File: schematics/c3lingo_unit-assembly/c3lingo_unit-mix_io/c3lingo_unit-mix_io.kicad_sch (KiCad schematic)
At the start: 45 parts, among them J201 Stage Line-In, J202 Mix Line-Out, J203 PowerSupply, J204 Ch1, J205 Ch2, J206 Ch3, SW201 GND Lift, U201 LM833-N, U202 DRV135UA, U203 LM833-N

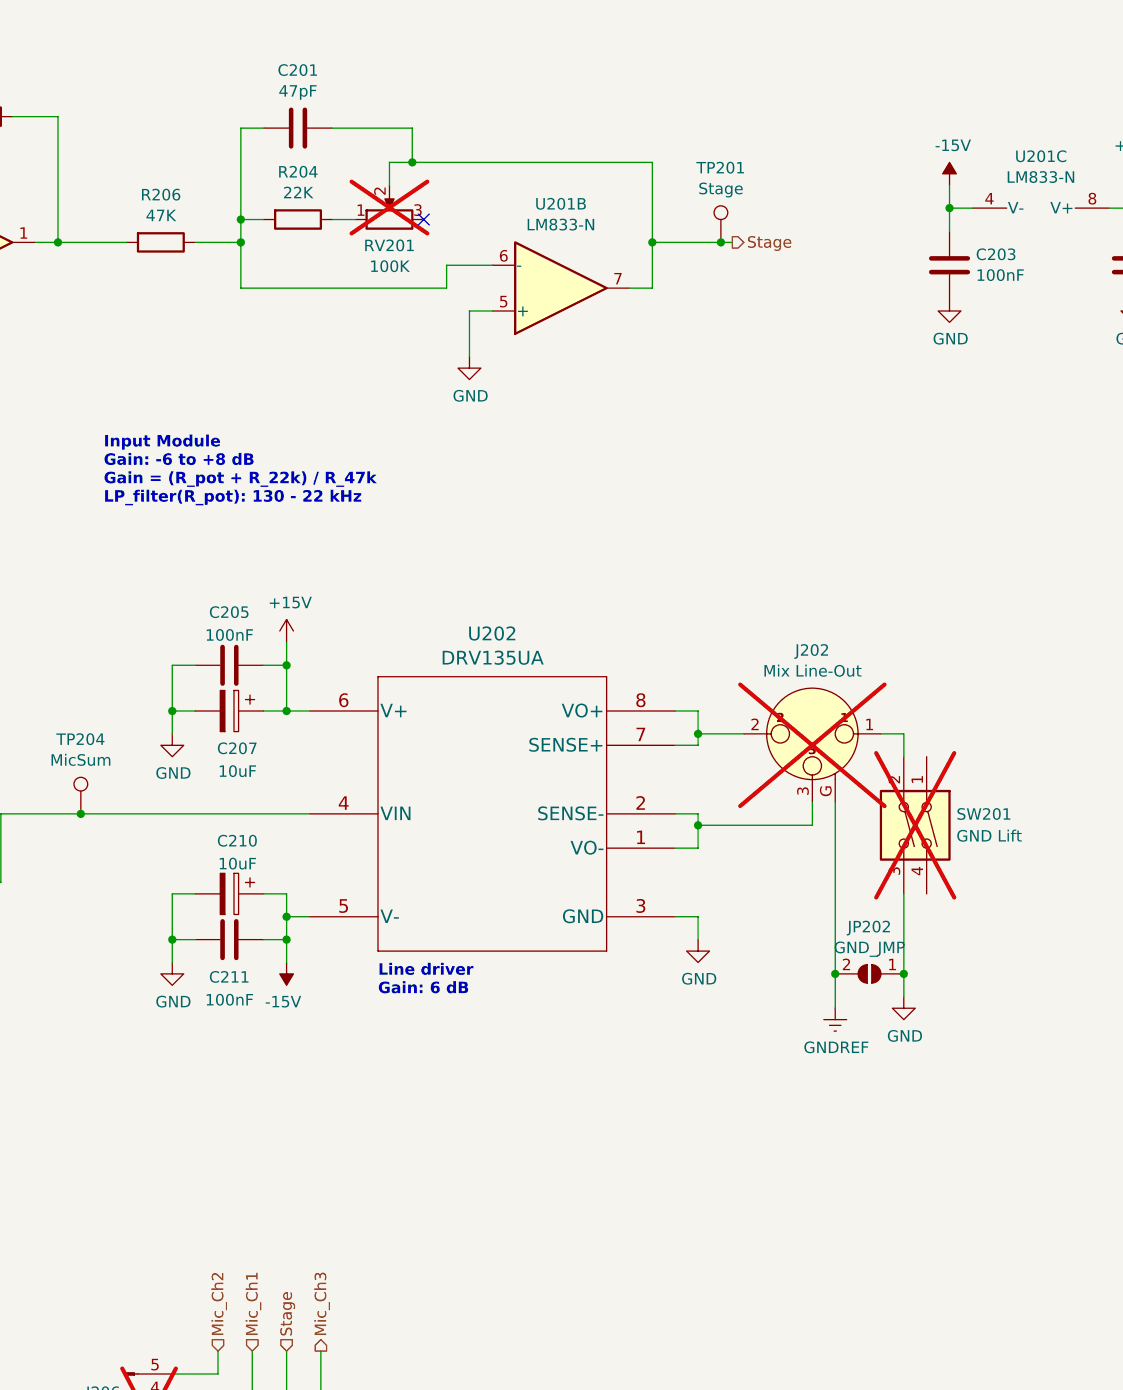
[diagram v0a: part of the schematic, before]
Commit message: Add rework to fix VU meter, muting delay, LP filters
Note: PCB files were not upated!

Changes/ required manual rework:
- Replace C314 with 100nF to reduce muting fade time
- Replace C301 with 680pF to have a 12 kHz low-pass filter on headphones
- Replace R309, R232, R335 to fix VU meter range (steps are a bit wonky
  afterwards, but top (and bottom) range are a lot more save now)
- Add 220pF in parallel to R602 to have a 10 kHz low-pass on microphone input

More rework is optional:
- Replace RV201 with a 10k (fixed) resistor (adjustment is not necessary)
- Replace R303 with 1k to reduce gain range from 45 to 34dB
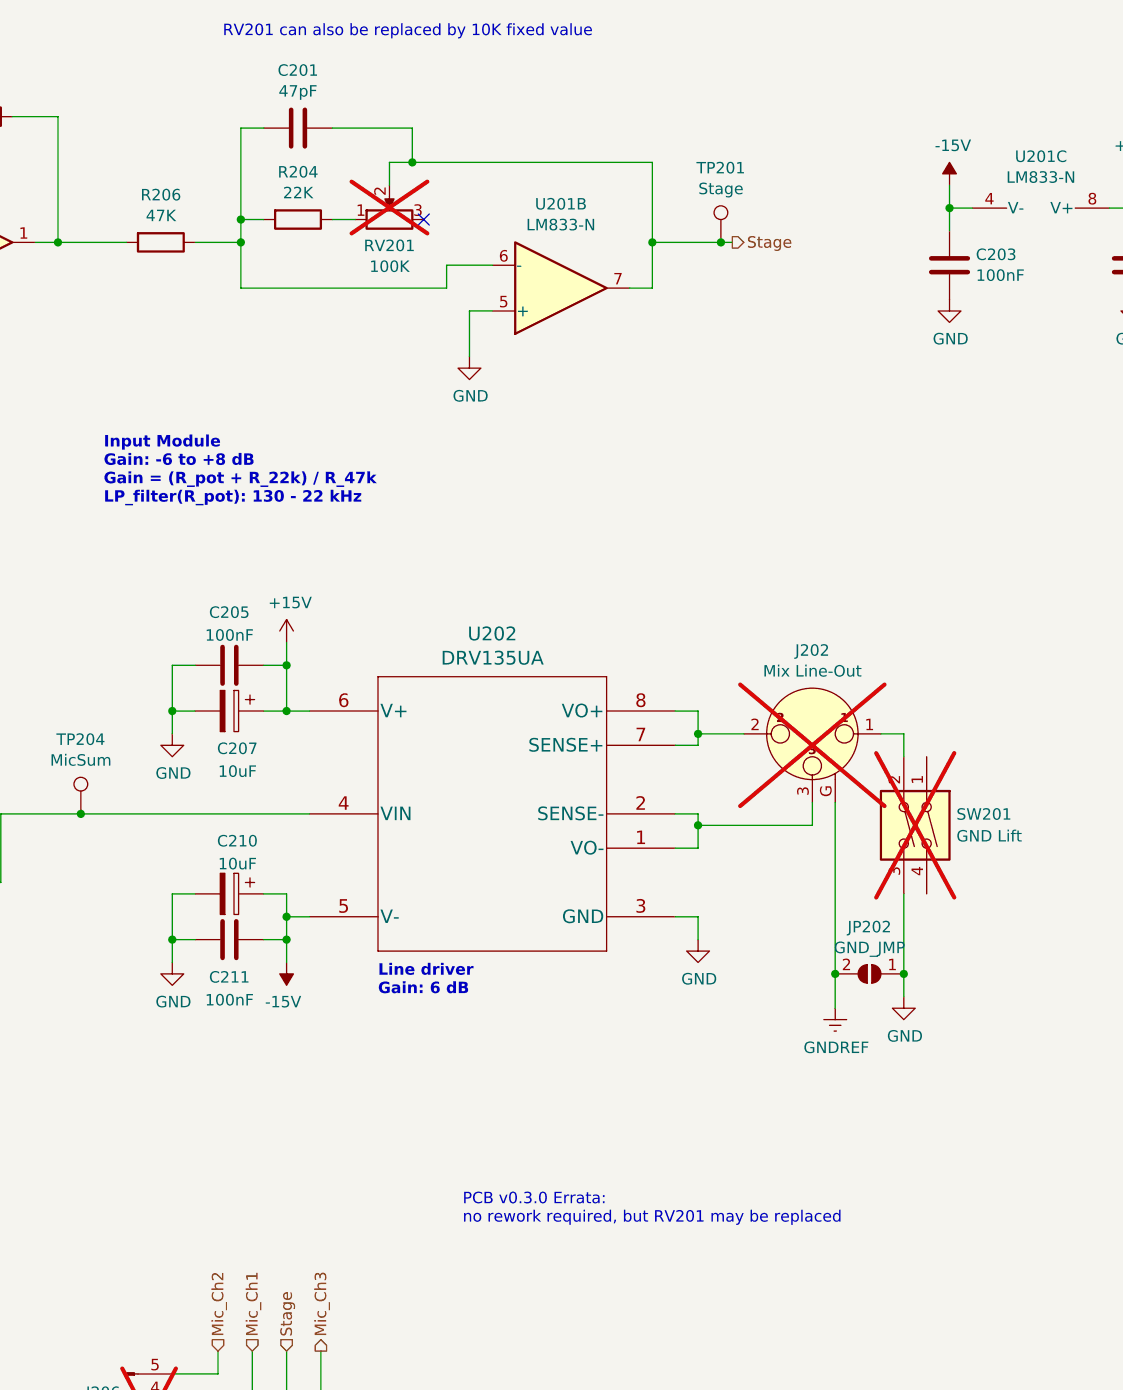
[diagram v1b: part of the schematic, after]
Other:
- note added: "PCB v0.3.0 Errata: no rework required, but RV201 may be replaced"
- note added: "RV201 can also be replaced by 10K fixed value"
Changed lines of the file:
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@@
 	(title_block
 		(title "c3lingo interpeter unit -- main I/O")
-		(date "2024-09-08")
-		(rev "v0.3.3")
+		(date "2024-11-16")
+		(rev "v0.3.4")
 		(company "Jannik Beyerstedt (jtbx)")
-		(comment 1 "Prototype 2")
+		(comment 1 "Prototype 2 + Rework")
 	)
 	(junction
@@
 		)
 	)
+	(text "PCB v0.3.0 Errata:\nno rework required, but RV201 may be replaced"
+		(exclude_from_sim no)
+		(at 177.038 158.242 0)
+		(effects
+			(font
+				(size 1.27 1.27)
+			)
+			(justify left)
+		)
+	)
 	(text "Line driver\nGain: 6 dB"
 		(exclude_from_sim no)
@@
 		)
 	)
+	(text "RV201 can also be replaced by 10K fixed value"
+		(exclude_from_sim no)
+		(at 170.942 27.432 0)
+		(effects
+			(font
+				(size 1.27 1.27)
+			)
+		)
+	)

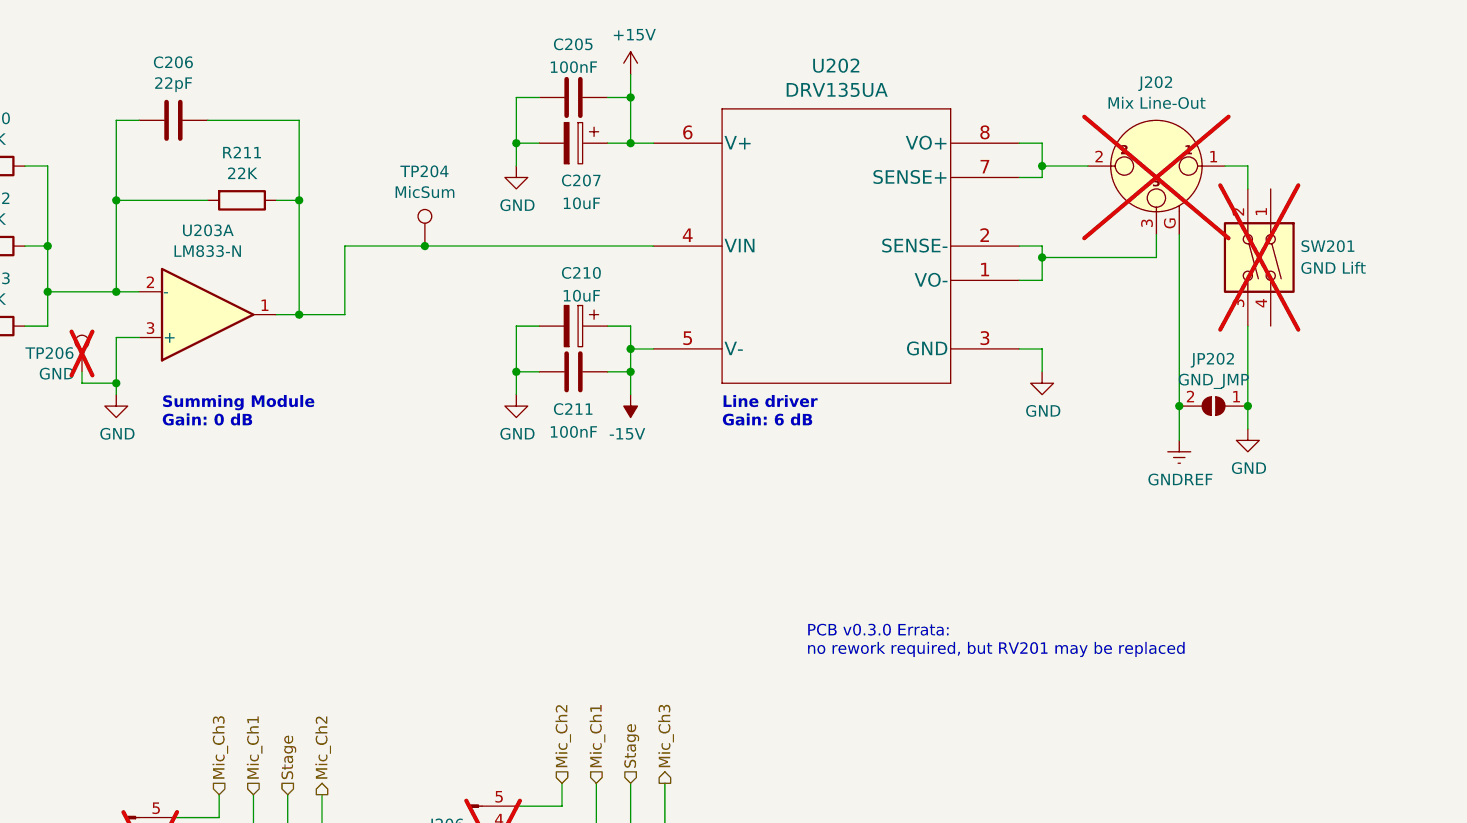
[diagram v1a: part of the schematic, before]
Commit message: Channel Mixer: Reduce mic and output gain
Note: Schematics not re-exported!
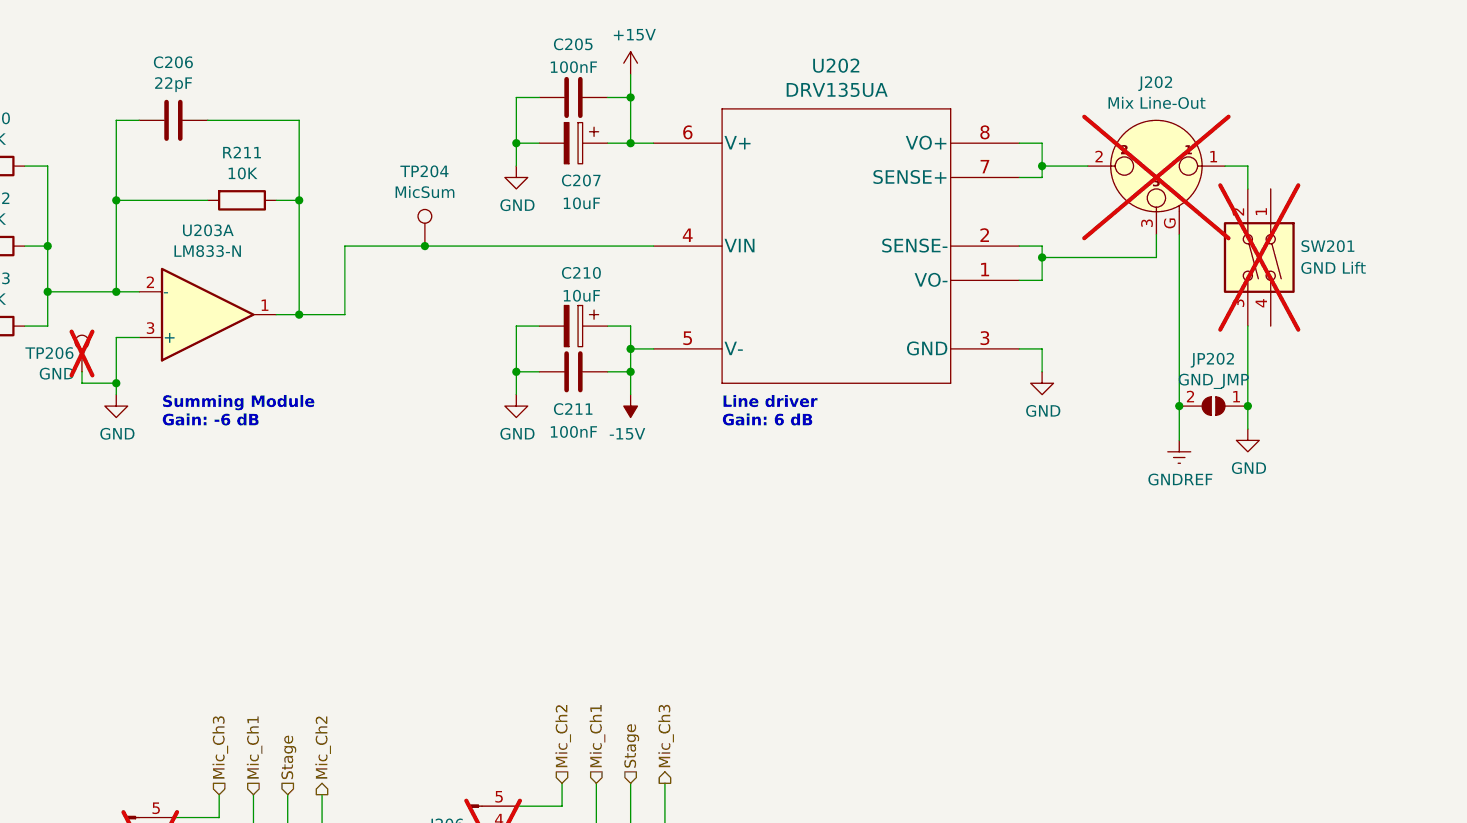
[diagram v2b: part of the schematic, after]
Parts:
- R211: value 22K -> 10K; LCSC Part # C17560 -> C17414
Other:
- note added: "Summing Module Gain: -6 dB"
- note removed: "PCB v0.3.0 Errata: no rework required, but RV201 may be replaced"
- note removed: "Summing Module Gain: 0 dB"
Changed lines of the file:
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@@
 	(title_block
 		(title "c3lingo interpeter unit -- main I/O")
-		(date "2024-11-16")
-		(rev "v0.3.4")
+		(date "2024-12-18")
+		(rev "v0.4.0-dev")
 		(company "Jannik Beyerstedt (jtbx)")
-		(comment 1 "Prototype 2 + Rework")
+		(comment 1 "Prototype 3")
 	)
 	(junction
@@
 		)
 	)
-	(text "PCB v0.3.0 Errata:\nno rework required, but RV201 may be replaced"
-		(exclude_from_sim no)
-		(at 177.038 158.242 0)
-		(effects
-			(font
-				(size 1.27 1.27)
-			)
-			(justify left)
-		)
-	)
 	(text "Line driver\nGain: 6 dB"
 		(exclude_from_sim no)
@@
 		)
 	)
-	(text "Summing Module\nGain: 0 dB"
+	(text "Summing Module\nGain: -6 dB"
 		(exclude_from_sim no)
 		(at 105.41 134.62 0)
@@
 		(shape input)
 		(at 115.57 175.26 90)
-		(fields_autoplaced yes)
 		(effects
 			(font
@@
 		(shape input)
 		(at 157.48 173.99 90)
-		(fields_autoplaced yes)
 		(effects
 			(font
@@
 		(shape output)
 		(at 161.29 173.99 90)
-		(fields_autoplaced yes)
 		(effects
 			(font
@@
 		(shape output)
 		(at 123.19 175.26 90)
-		(fields_autoplaced yes)
 		(effects
 			(font
@@
 		(shape input)
 		(at 119.38 175.26 90)
-		(fields_autoplaced yes)
 		(effects
 			(font
@@
 		(shape input)
 		(at 149.86 173.99 90)
-		(fields_autoplaced yes)
 		(effects
 			(font
@@
 		(shape input)
 		(at 81.28 175.26 90)
-		(fields_autoplaced yes)
 		(effects
 			(font
@@
 		(shape input)
 		(at 77.47 175.26 90)
-		(fields_autoplaced yes)
 		(effects
 			(font
@@
 		(shape output)
 		(at 207.01 50.8 0)
-		(fields_autoplaced yes)
 		(effects
 			(font
@@
 		(shape input)
 		(at 74.93 114.3 180)
-		(fields_autoplaced yes)
 		(effects
 			(font
@@
 		(shape input)
 		(at 74.93 123.19 180)
-		(fields_autoplaced yes)
 		(effects
 			(font
@@
 		(shape output)
 		(at 85.09 175.26 90)
-		(fields_autoplaced yes)
 		(effects
 			(font
@@
 		(shape input)
 		(at 74.93 105.41 180)
-		(fields_autoplaced yes)
 		(effects
 			(font
@@
 		(shape input)
 		(at 73.66 175.26 90)
-		(fields_autoplaced yes)
 		(effects
 			(font
@@
 		(shape input)
 		(at 153.67 173.99 90)
-		(fields_autoplaced yes)
 		(effects
 			(font
@@
 		(shape input)
 		(at 111.76 175.26 90)
-		(fields_autoplaced yes)
 		(effects
 			(font
@@
 			)
 		)
-		(property "Value" "22K"
+		(property "Value" "10K"
 			(at 114.3 106.2736 90)
 			(effects
@@
 			)
 		)
-		(property "LCSC Part #" "C17560"
+		(property "LCSC Part #" "C17414"
 			(at 114.3 109.22 0)
 			(effects
